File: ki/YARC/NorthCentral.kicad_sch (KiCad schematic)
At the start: 3 parts, among them U102 74HC245, U103 74HC245

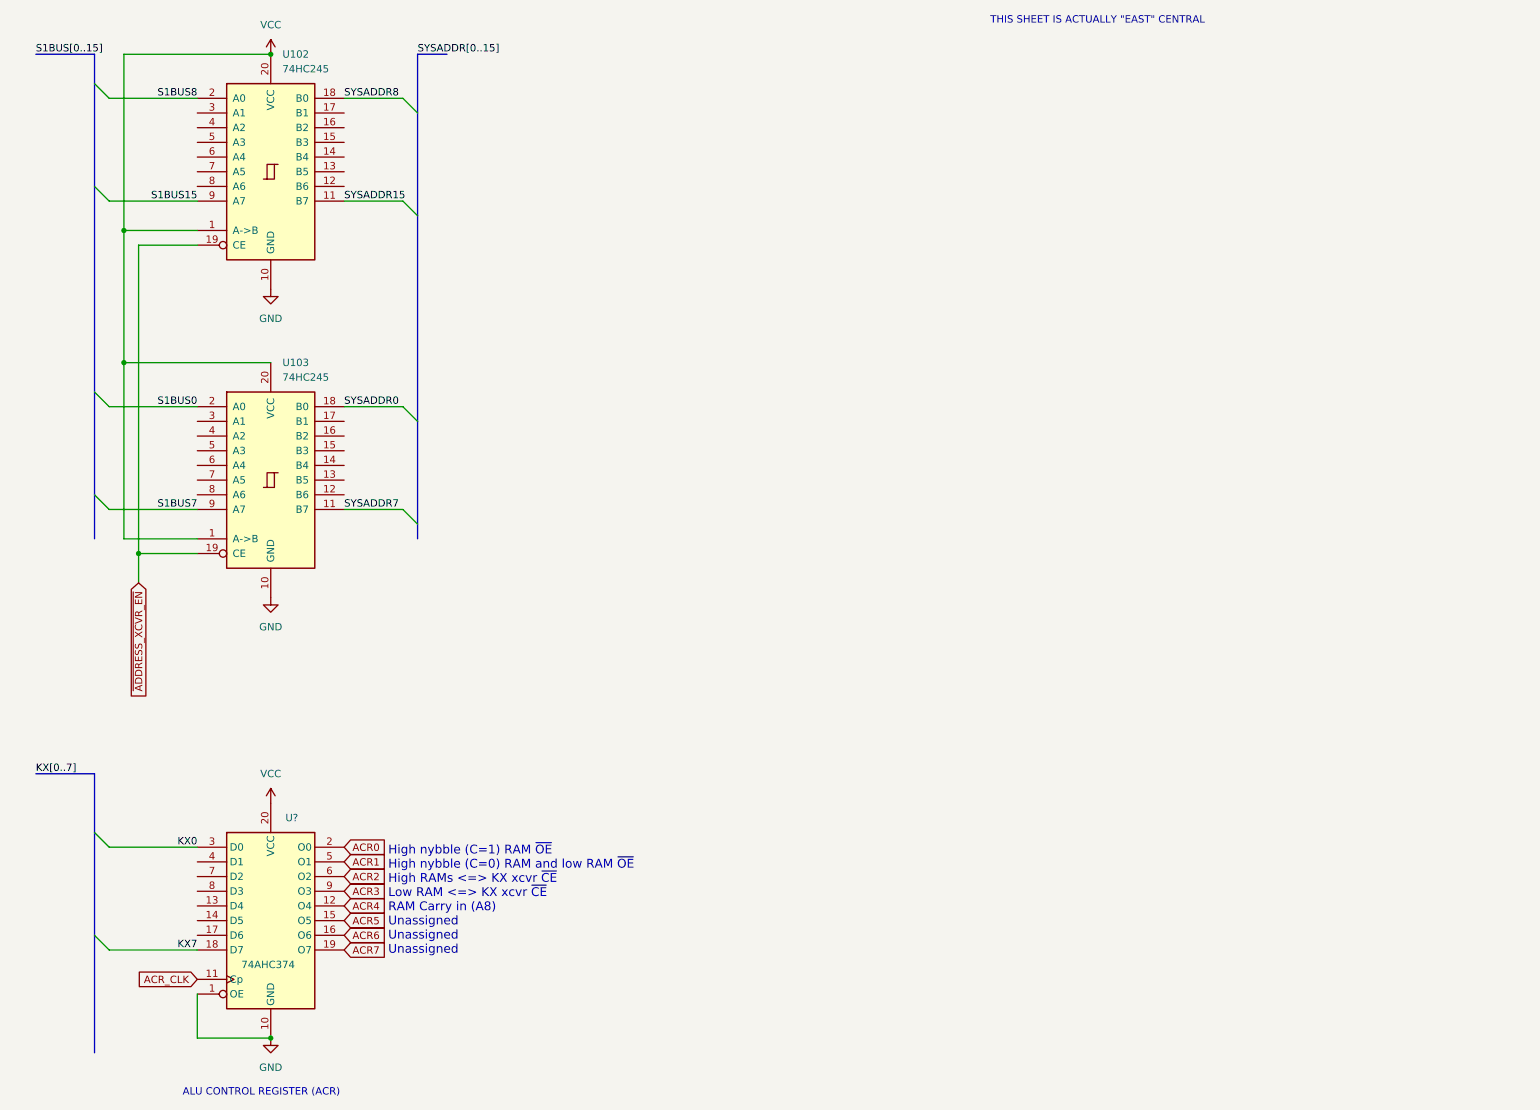
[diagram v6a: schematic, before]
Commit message: Redesign of ALU control logic
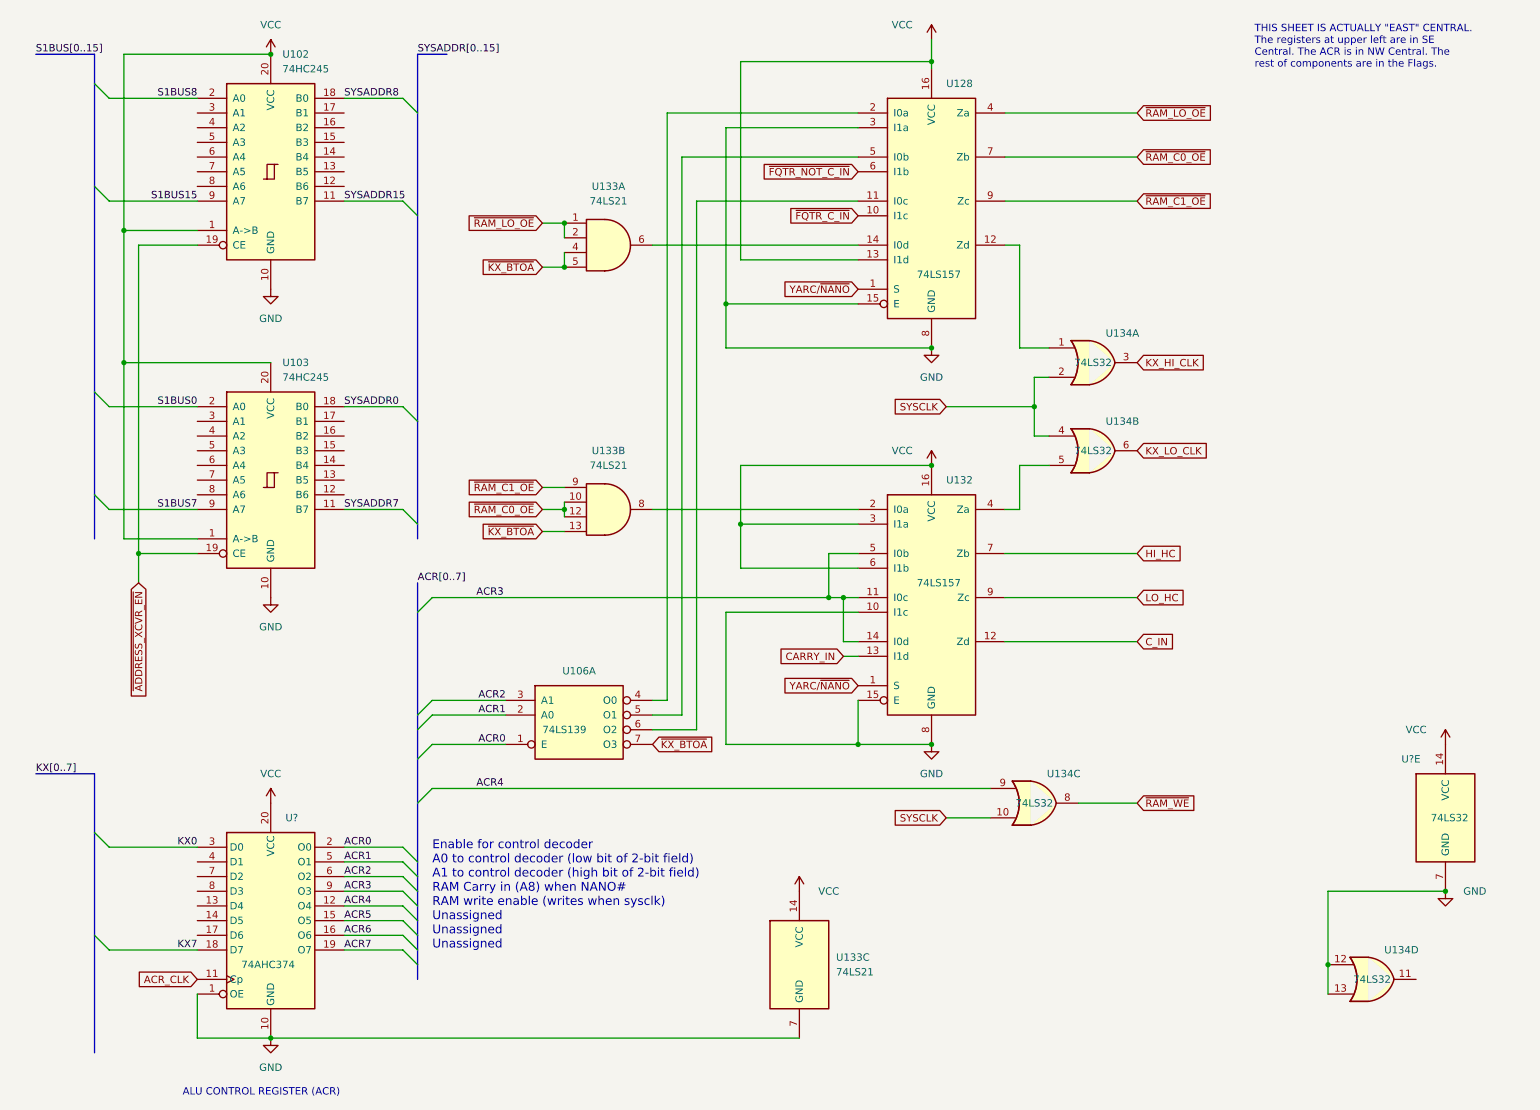
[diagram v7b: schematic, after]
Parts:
- added U106: 74LS139, symbol 74xx:74LS139
- added U128, U132: 74LS157, symbol 74xx:74LS157
- added U133: 74LS21, symbol 74xx:74LS21
- added U134, U?: 74LS32, symbol 74xx:74LS32
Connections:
- net ACR0: now also U106.1 (E)
- net ACR1: now also U106.2 (A0)
- net ACR2: now also U106.3 (A1)
- net ACR3: now also U132.11 (I0c), U132.14 (I0d), U132.5 (I0b)
- net ACR4: now also U134.9
- net GND: now also U128.15 (E), U128.3 (I1a), U128.8 (GND), U132.10 (I1c), U132.15 (E), U132.8 (GND), U133.7 (GND), U134.12, U134.13, U?.7 (GND)
- net VCC: now also U128.13 (I1d), U128.16 (VCC), U132.16 (VCC), U132.3 (I1a), U132.6 (I1b), U133.14 (VCC), U?.14 (VCC)
- new net: U132.2 (I0a), U133.8
- new net: U132.4 (Za), U134.5
- new net: U128.12 (Zd), U134.1
- new net: U106.4 (O0), U128.2 (I0a)
- new net: U106.5 (O1), U128.5 (I0b)
- new net: U106.6 (O2), U128.11 (I0c)
- new net: U128.14 (I0d), U133.6
- new net CARRY_IN: U132.13 (I1d)
- new net C_IN: U132.12 (Zd)
- new net HI_HC: U132.7 (Zb)
- new net KX_HI_CLK: U134.3
- new net KX_LO_CLK: U134.6
- new net LO_HC: U132.9 (Zc)
- new net SYSCLK: U134.10, U134.2, U134.4
- new net YARC/~{NANO}: U128.1 (S), U132.1 (S)
- new net ~{FQTR_C_IN}: U128.10 (I1c)
- new net ~{FQTR_NOT_C_IN}: U128.6 (I1b)
- new net ~{KX_BTOA}: U106.7 (O3), U133.13, U133.4, U133.5
- new net ~{RAM_C0_OE}: U128.7 (Zb), U133.10, U133.12
- new net ~{RAM_C1_OE}: U128.9 (Zc), U133.9
- new net ~{RAM_LO_OE}: U128.4 (Za), U133.1, U133.2
- new net ~{RAM_WE}: U134.8
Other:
- note added: "Enable for control decoder A0 to control decoder (low bit of 2-bit field) A1 to control decoder (high bit of 2-bit field) RAM Carry in (A8) when NANO# RAM write enable (writes when sysclk) Unassigned Unassigned Unassigned"
- note added: "THIS SHEET IS ACTUALLY "EAST" CENTRAL. The registers at upper left are in SE Central. The ACR is in NW Central. The rest of components are in the Flags."
- note removed: "High nybble (C=1) RAM ~{OE} High nybble (C=0) RAM and low RAM ~{OE} High RAMs <=> KX xcvr ~{CE} Low RAM <=> KX xcvr ~{CE} RAM Carry in (A8) Unassigned Unassigned Unassigned"
- note removed: "THIS SHEET IS ACTUALLY "EAST" CENTRAL"

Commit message: Yet more cleanup on ALU and flags design
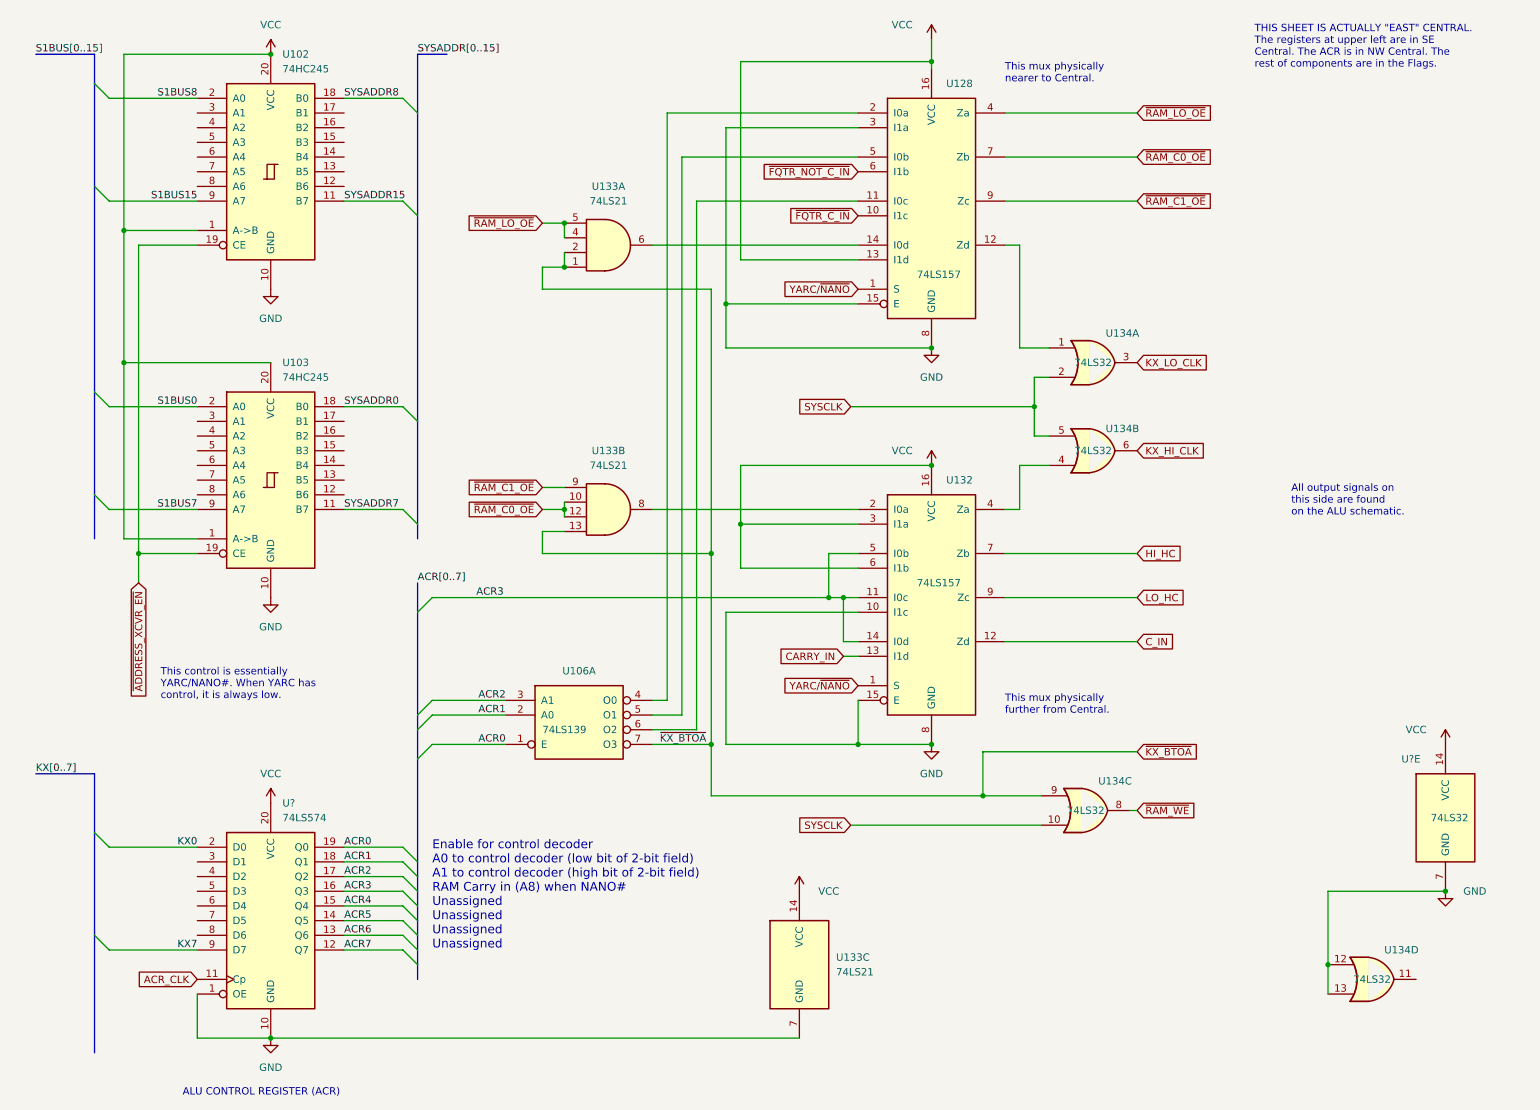
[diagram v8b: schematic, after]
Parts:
- removed U?: 74AHC374, symbol 74xx:74AHC374
- added U?: 74LS574, symbol 74xx:74LS574
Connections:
- net ACR0: now also U?.19 (Q0)
- net ACR1: now also U?.18 (Q1)
- net ACR2: now also U?.17 (Q2)
- net ACR3: now also U?.16 (Q3)
- net ACR4: now also U?.15 (Q4); no longer U134.9
- net ACR5: now also U?.14 (Q5)
- net ACR6: now also U?.13 (Q6)
- net ACR7: now also U?.12 (Q7)
- net ACR_CLK: now also U?.11 (Cp)
- net GND: now also U?.1 (OE), U?.10 (GND)
- net KX0: now also U?.2 (D0)
- net KX7: now also U?.9 (D7)
- net KX_HI_CLK: now also U134.6; no longer U134.3
- net KX_LO_CLK: now also U134.3; no longer U134.6
- net SYSCLK: now also U134.5; no longer U134.4
- net VCC: now also U?.20 (VCC)
- net ~{KX_BTOA}: now also U133.1, U133.2, U134.9; no longer U133.4, U133.5
- net ~{RAM_LO_OE}: now also U133.4, U133.5; no longer U133.1, U133.2
- net at U132.4 (Za): now also U134.4; no longer U134.5
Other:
- note added: "All output signals on this side are found on the ALU schematic."
- note added: "Enable for control decoder A0 to control decoder (low bit of 2-bit field) A1 to control decoder (high bit of 2-bit field) RAM Carry in (A8) when NANO# Unassigned Unassigned Unassigned Unassigned"
- note added: "This control is essentially YARC/NANO#. When YARC has control, it is always low."
- note added: "This mux physically further from Central."
- note added: "This mux physically nearer to Central."
- note removed: "Enable for control decoder A0 to control decoder (low bit of 2-bit field) A1 to control decoder (high bit of 2-bit field) RAM Carry in (A8) when NANO# RAM write enable (writes when sysclk) Unassigned Unassigned Unassigned"
- moved on the sheet: U134C
